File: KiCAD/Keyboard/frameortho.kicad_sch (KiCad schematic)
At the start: 0 parts

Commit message: move vbus capacitor
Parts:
- added U1: RP2040, Package_DFN_QFN:QFN-56-1EP_7x7mm_P0.4mm_EP3.2x3.2mm, symbol MCU_RaspberryPi:RP2040
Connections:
- new net: U1.1 (IOVDD), U1.10 (IOVDD), U1.22 (IOVDD), U1.33 (IOVDD), U1.42 (IOVDD), U1.49 (IOVDD)
- new net: U1.23 (DVDD), U1.50 (DVDD)
- new net D_N: U1.46 (USB_DM)
- new net D_P: U1.47 (USB_DP)
- new net GND: U1.57 (GND)
- new net X_IN: U1.20 (XIN)
- new net X_OUT: U1.21 (XOUT)
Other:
- added sheet matrix (matrix.kicad_sch)

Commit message: start keyboard pcb
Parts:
- added C1, C11, C2: 1µF, Capacitor_SMD:C_0402_1005Metric, symbol Device:C_Small
- added C10, C12, C13, C3, C4, C5, C6, C7, C8, C9: 100nF, Capacitor_SMD:C_0402_1005Metric, symbol Device:C_Small
- added C14, C15: 33pF, Capacitor_SMD:C_0402_1005Metric, symbol Device:C_Small
- added J1: USB_C_Receptacle_USB2.0_16P, ScottoKeebs_Components:USB_C_HRO_TYPE-C-31-M-14, symbol Connector:USB_C_Receptacle_USB2.0_16P
- added R1, R2, R5, R7, R8: 5.1kΩ, Resistor_SMD:R_0402_1005Metric, symbol Device:R_Small
- added R3, R4: 27Ω, Resistor_SMD:R_0402_1005Metric, symbol Device:R_Small
- added R6, R9: 1kΩ, Resistor_SMD:R_0402_1005Metric, symbol Device:R_Small
- added SW1, SW2: SW_Push, ScottoKeebs_Components:Button_TL3342, symbol Switch:SW_Push
- added U2: W25Q128JVS, Package_SO:SOIC-8_5.3x5.3mm_P1.27mm, symbol Memory_Flash:W25Q128JVS
- added U3: XC6206PxxxMR, Package_TO_SOT_SMD:SOT-23-3, symbol Regulator_Linear:XC6206PxxxMR
- added Y1: 12 MHz 20pF, Crystal:Crystal_SMD_Abracon_ABM3B-4Pin_5.0x3.2mm, symbol Device:Crystal_GND24_Small
- U1: symbol MCU_RaspberryPi:RP2040 -> Custom:RP2040
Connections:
- net D_N: now also J1.A7 (D-), J1.B7 (D-), R4.2; no longer U1.46 (USB_DM)
- net D_P: now also J1.A6 (D+), J1.B6 (D+), R3.2; no longer U1.47 (USB_DP)
- net GND: now also U1.19 (TESTEN), C1.2, C10.2, C11.2, C12.2, C13.2, C14.1, C15.1, C2.2, C3.2, C4.2, C5.2, C6.2, C7.2, C8.2, C9.2, J1.A1 (GND), J1.A12 (GND), J1.B1 (GND), J1.B12 (GND), J1.S1 (SHIELD), R1.1, R2.1, SW1.1, SW2.1, U2.4 (GND), U3.1 (GND), Y1.2, Y1.4
- net X_IN: now also C14.2, Y1.1
- net X_OUT: now also R6.2
- net +3V3: now reaches U1.1 (IOVDD), U1.10 (IOVDD), U1.22 (IOVDD), U1.33 (IOVDD), U1.42 (IOVDD), U1.49 (IOVDD)
- net +3V3: now also U1.43 (ADC_AVDD), U1.44 (VREG_IN), U1.48 (USB_VDD), C1.1, C10.1, C2.1, C3.1, C4.1, C5.1, C6.1, C7.1, C8.1, C9.1, R5.1, R7.1, U2.8 (VCC), U3.2 (VO)
- net +1V1: now reaches U1.23 (DVDD), U1.50 (DVDD)
- net +1V1: now also U1.45 (VREG_VOUT), C11.1, C12.1, C13.1
- net SWCLK: now reaches U1.24 (SWCLK)
- net SWDIO: now reaches U1.25 (SWD)
- net RUN: now reaches U1.26 (RUN)
- net RUN: now also R7.2, SW1.2
- net SD3: now reaches U1.51 (QSPI_SD3)
- net SD3: now also U2.7 (~{HOLD}/~{RESET}/IO_{3})
- net SCLK: now reaches U1.52 (QSPI_SCLK)
- net SCLK: now also U2.6 (CLK)
- net SDO: now reaches U1.53 (QSPI_SD0)
- net SDO: now also U2.5 (DI/IO_{0})
- net SD2: now reaches U1.54 (QSPI_SD2)
- net SD2: now also U2.3 (~{WP}/IO_{2})
- net SD1: now reaches U1.55 (QSPI_SD1)
- net SD1: now also U2.2 (DO/IO_{1})
- net SEL: now reaches U1.56 (QSPI_SS)
- net SEL: now also R8.2, R9.2, U2.1 (~{CS})
- new net: J1.B5 (CC2), R2.2
- new net: R4.1, U1.46 (USB_D_N)
- new net: R3.1, U1.47 (USB_D_P)
- new net: C15.2, R6.1, Y1.3
- new net: R5.2, R8.1
- new net: R9.1, SW2.2
- new net: J1.A5 (CC1), R1.2
- new net +5V: J1.A4 (VBUS), J1.A9 (VBUS), J1.B4 (VBUS), J1.B9 (VBUS), U3.3 (VI)
- no-connect marks 0 -> 2
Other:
- note added: "C(L)=2*(C(Xtal)-C(Stray))=2*(20-4)=32pF->33pF"
- note added: "C11 is for VREG_OUT/Pin 45"
- note added: "C2 is for VREG_IN/Pin 44"
- moved on the sheet: U1

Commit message: mostly finished pcb
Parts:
- removed J1: USB_C_Receptacle_USB2.0_16P, ScottoKeebs_Components:USB_C_HRO_TYPE-C-31-M-14, symbol Connector:USB_C_Receptacle_USB2.0_16P
- removed R1, R2: 5.1kΩ, Resistor_SMD:R_0402_1005Metric, symbol Device:R_Small
- added TP17, TP18, TP19, TP20: TestPoint, TestPoint:TestPoint_Pad_D2.0mm, symbol Connector:TestPoint
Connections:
- net +5V: now also TP17.1
- net COL_0: now also U1.2 (GPIO0)
- net COL_1: now also U1.3 (GPIO1)
- net COL_2: now also U1.4 (GPIO2)
- net COL_3: now also U1.5 (GPIO3)
- net COL_4: now also U1.6 (GPIO4)
- net COL_5: now also U1.31 (GPIO20)
- net COL_6: now also U1.30 (GPIO19)
- net COL_7: now also U1.29 (GPIO18)
- net COL_8: now also U1.28 (GPIO17)
- net COL_9: now also U1.27 (GPIO16)
- net D_N: now also TP19.1
- net D_P: now also TP18.1
- net GND: now also TP20.1
- net ROW_0: now also U1.41 (GPIO29_ADC3)
- net ROW_1: now also U1.40 (GPIO28_ADC2)
- net ROW_2: now also U1.39 (GPIO27_ADC1)
- net ROW_3: now also U1.38 (GPIO26_ADC0)
- net GPIO8: now reaches U1.11 (GPIO8)
- net GPIO9: now reaches U1.12 (GPIO9)
- net GPIO10: now reaches U1.13 (GPIO10)
- net GPIO11: now reaches U1.14 (GPIO11)
- net GPIO12: now reaches U1.15 (GPIO12)
- net GPIO13: now reaches U1.16 (GPIO13)
- net GPIO14: now reaches U1.17 (GPIO14)
- net GPIO15: now reaches U1.18 (GPIO15)
- net GPIO21: now reaches U1.32 (GPIO21)
- net GPIO22: now reaches U1.34 (GPIO22)
- net GPIO23: now reaches U1.35 (GPIO23)
- net GPIO24: now reaches U1.36 (GPIO24)
- net GPIO25: now reaches U1.37 (GPIO25)
- net GPIO5: now reaches U1.7 (GPIO5)
- net GPIO6: now reaches U1.8 (GPIO6)
- net GPIO7: now reaches U1.9 (GPIO7)
- no-connect marks 2 -> 0
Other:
- added sheet pads (pads.kicad_sch)
- note added: "Boot"
- note added: "Buttons"
- note added: "Capacitors"
- note added: "Crystal"
- note added: "Flash"
- note added: "RP2040"
- note added: "Regulator"
- note added: "Reset"
- note added: "USB Pads"
- moved on the sheet: C1, C10, C11, C12, C13, C14, C15, C2, C3, C4, C5, C6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

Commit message: idk what i did tbh
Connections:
- net GPIO21 is gone; now on net COL_9: U1.32 (GPIO21)
- net GPIO22 is gone; now on net COL_8: U1.34 (GPIO22)
- net GPIO23 is gone; now on net COL_7: U1.35 (GPIO23)
- net GPIO24 is gone; now on net COL_6: U1.36 (GPIO24)
- net GPIO25 is gone; now on net COL_5: U1.37 (GPIO25)
- net COL_5: no longer U1.31 (GPIO20)
- net COL_6: no longer U1.30 (GPIO19)
- net COL_7: no longer U1.29 (GPIO18)
- net COL_8: no longer U1.28 (GPIO17)
- net COL_9: no longer U1.27 (GPIO16)
- new net GPIO16: U1.27 (GPIO16)
- new net GPIO17: U1.28 (GPIO17)
- new net GPIO18: U1.29 (GPIO18)
- new net GPIO19: U1.30 (GPIO19)
- new net GPIO20: U1.31 (GPIO20)

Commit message: why no commit
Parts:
- added C16: 1µF, Capacitor_SMD:C_0402_1005Metric, symbol Device:C_Small
- C14, C15: value 33pF -> 27pF
- Y1: value 12 MHz 20pF -> 12 MHz 18pF
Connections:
- net +5V: now also C16.1
- net GND: now also C16.2
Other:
- note added: "C(L)=2*(C(Xtal)-C(Stray))=2*(18-5)=26pF->27pF"
- note removed: "C(L)=2*(C(Xtal)-C(Stray))=2*(20-4)=32pF->33pF"
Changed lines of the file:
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@@
 		)
 	)
-	(text "C(L)=2*(C(Xtal)-C(Stray))=2*(20-4)=32pF->33pF"
+	(text "C(L)=2*(C(Xtal)-C(Stray))=2*(18-5)=26pF->27pF"
 		(exclude_from_sim no)
 		(at 228.6 259.334 0)
@@
 	)
 	(junction
+		(at 245.11 102.87)
+		(diameter 0)
+		(color 0 0 0 0)
+	)
+	(junction
+		(at 255.27 110.49)
+		(diameter 0)
+		(color 0 0 0 0)
+	)
+	(junction
 		(at 182.88 102.87)
 		(diameter 0)
@@
 	(wire
 		(pts
+			(xy 245.11 104.14) (xy 245.11 102.87)
+		)
+		(stroke
+			(width 0)
+			(type default)
+		)
+	)
+	(wire
+		(pts
 			(xy 139.7 186.69) (xy 149.86 186.69)
 		)
@@
 	(wire
 		(pts
+			(xy 245.11 102.87) (xy 247.65 102.87)
+		)
+		(stroke
+			(width 0)
+			(type default)
+		)
+	)
+	(wire
+		(pts
 			(xy 128.27 31.75) (xy 140.97 31.75)
 		)
@@
 	(wire
 		(pts
+			(xy 245.11 110.49) (xy 255.27 110.49)
+		)
+		(stroke
+			(width 0)
+			(type default)
+		)
+	)
+	(wire
+		(pts
+			(xy 245.11 109.22) (xy 245.11 110.49)
+		)
+		(stroke
+			(width 0)
+			(type default)
+		)
+	)
+	(wire
+		(pts
 			(xy 139.7 179.07) (xy 149.86 179.07)
 		)
@@
 	(wire
 		(pts
-			(xy 242.57 102.87) (xy 247.65 102.87)
+			(xy 242.57 102.87) (xy 245.11 102.87)
 		)
 		(stroke
@@
 			)
 		)
-		(property "Value" "12 MHz 20pF"
+		(property "Value" "12 MHz 18pF"
 			(at 233.68 239.3882 0)
 			(effects
@@
 			)
 		)
-		(property "Value" "33pF"
+		(property "Value" "27pF"
 			(at 217.17 246.3735 0)
 			(effects
@@
 			)
 		)
-		(property "Value" "33pF"
+		(property "Value" "27pF"
 			(at 229.87 250.698 0)
 			(effects
@@
 					(unit 1)
 				)
+			)
+		)
+	)
+	(symbol
+		(lib_id "Device:C_Small")
+		(at 245.11 106.68 0)
+		(mirror y)
+		(unit 1)
+		(exclude_from_sim no)
+		(in_bom yes)
+		(on_board yes)
+		(dnp no)
+		(property "Reference" "C16"
+			(at 242.57 105.4162 0)
+			(effects
+				(font
+					(size 1.27 1.27)
+				)
+				(justify left)
+			)
+		)
+		(property "Value" "1µF"
+			(at 242.57 107.9562 0)
+			(effects
+				(font
+					(size 1.27 1.27)
+				)
+				(justify left)
+			)
+		)
+		(property "Footprint" "Capacitor_SMD:C_0402_1005Metric"
+			(at 245.11 106.68 0)
+			(effects
+				(font
+					(size 1.27 1.27)
+				)
+				(hide yes)
+			)
+		)
+		(property "Datasheet" "~"
+			(at 245.11 106.68 0)
+			(effects
+				(font
+					(size 1.27 1.27)
+				)
+				(hide yes)
+			)
+		)
+		(property "Description" "Unpolarized capacitor, small symbol"
+			(at 245.11 106.68 0)
+			(effects
+				(font
+					(size 1.27 1.27)
+				)
+				(hide yes)
+			)
+		)
+		(pin "1"
+		)
+		(pin "2"
+		)
+		(instances
+			(project "frameortho"
+				(path "/a3a2616b-6905-4b87-92b2-8451542cf464"
+					(reference "C16")
+					(unit 1)
+				)

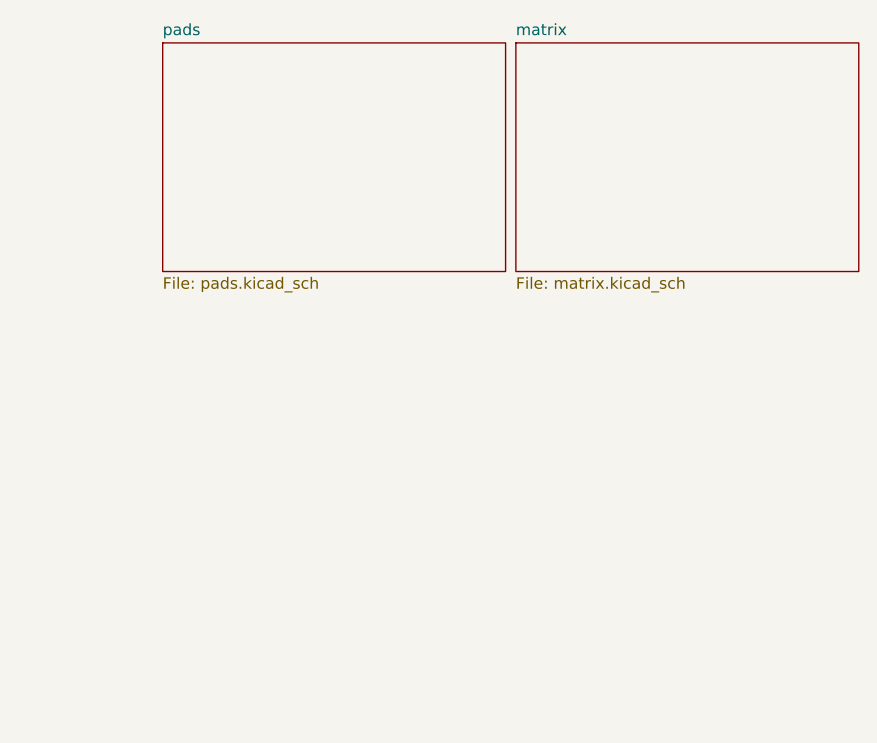
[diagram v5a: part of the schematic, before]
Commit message: mounting holes
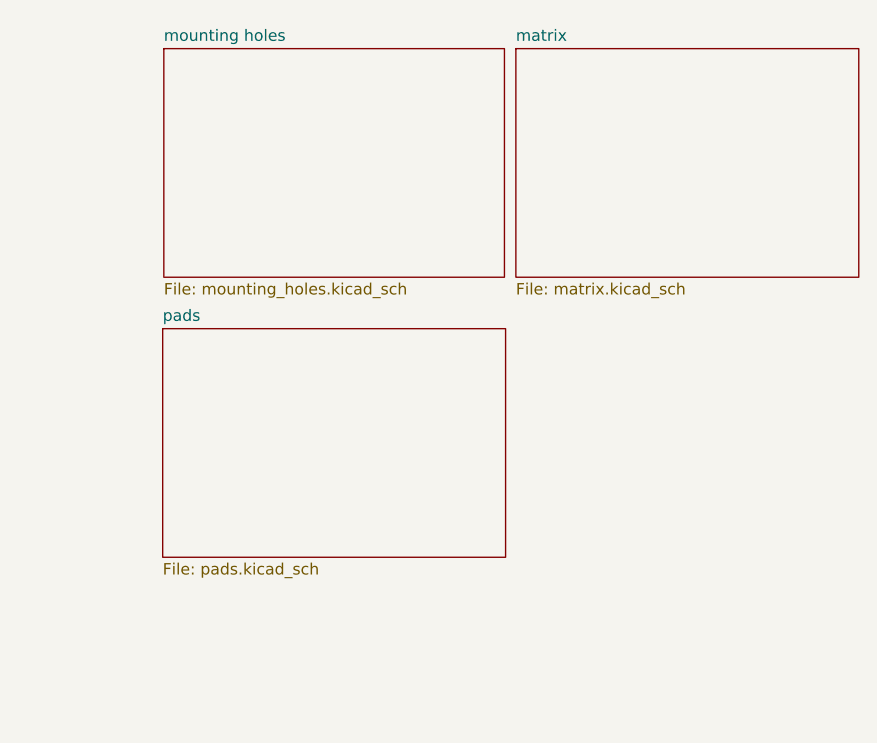
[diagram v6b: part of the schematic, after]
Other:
- added sheet mounting holes (mounting_holes.kicad_sch)
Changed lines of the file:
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@@
 	)
 	(sheet
-		(at 367.03 15.24)
+		(at 367.03 15.875)
 		(size 38.1 25.4)
 		(exclude_from_sim no)
@@
 		)
 		(property "Sheetname" "matrix"
-			(at 367.03 14.5284 0)
+			(at 367.03 15.1634 0)
 			(effects
 				(font
@@
 		)
 		(property "Sheetfile" "matrix.kicad_sch"
-			(at 367.03 41.2246 0)
+			(at 367.03 41.8596 0)
 			(effects
 				(font
@@
 	)
 	(sheet
-		(at 327.787 15.24)
+		(at 327.914 15.875)
+		(size 37.846 25.4)
+		(exclude_from_sim no)
+		(in_bom yes)
+		(on_board yes)
+		(dnp no)
+		(fields_autoplaced yes)
+		(stroke
+			(width 0.1524)
+			(type solid)
+		)
+		(fill
+			(color 0 0 0 0.0000)
+		)
+		(property "Sheetname" "mounting holes"
+			(at 327.914 15.1634 0)
+			(effects
+				(font
+					(size 1.27 1.27)
+				)
+				(justify left bottom)
+			)
+		)
+		(property "Sheetfile" "mounting_holes.kicad_sch"
+			(at 327.914 41.8596 0)
+			(effects
+				(font
+					(size 1.27 1.27)
+				)
+				(justify left top)
+			)
+		)
+		(instances
+			(project "frameortho"
+				(path "/a3a2616b-6905-4b87-92b2-8451542cf464"
+					(page "4")
+				)
+			)
+		)
+	)
+	(sheet
+		(at 327.787 46.99)
 		(size 38.1 25.4)
 		(exclude_from_sim no)
@@
 		)
 		(property "Sheetname" "pads"
-			(at 327.787 14.5284 0)
+			(at 327.787 46.2784 0)
 			(effects
 				(font
@@
 		)
 		(property "Sheetfile" "pads.kicad_sch"
-			(at 327.787 41.2246 0)
+			(at 327.787 72.9746 0)
 			(effects
 				(font
